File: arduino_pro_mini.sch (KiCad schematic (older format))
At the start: 19 parts, among them J1 CONN_06RA, J2 CONN_12, J3 CONN_02, J4 CONN_02, J5 CONN_12, SW1 SW_Push, U1 MIC5205-2.5YM5, U2 ATmega328-AU, Y1 Resonator_Small

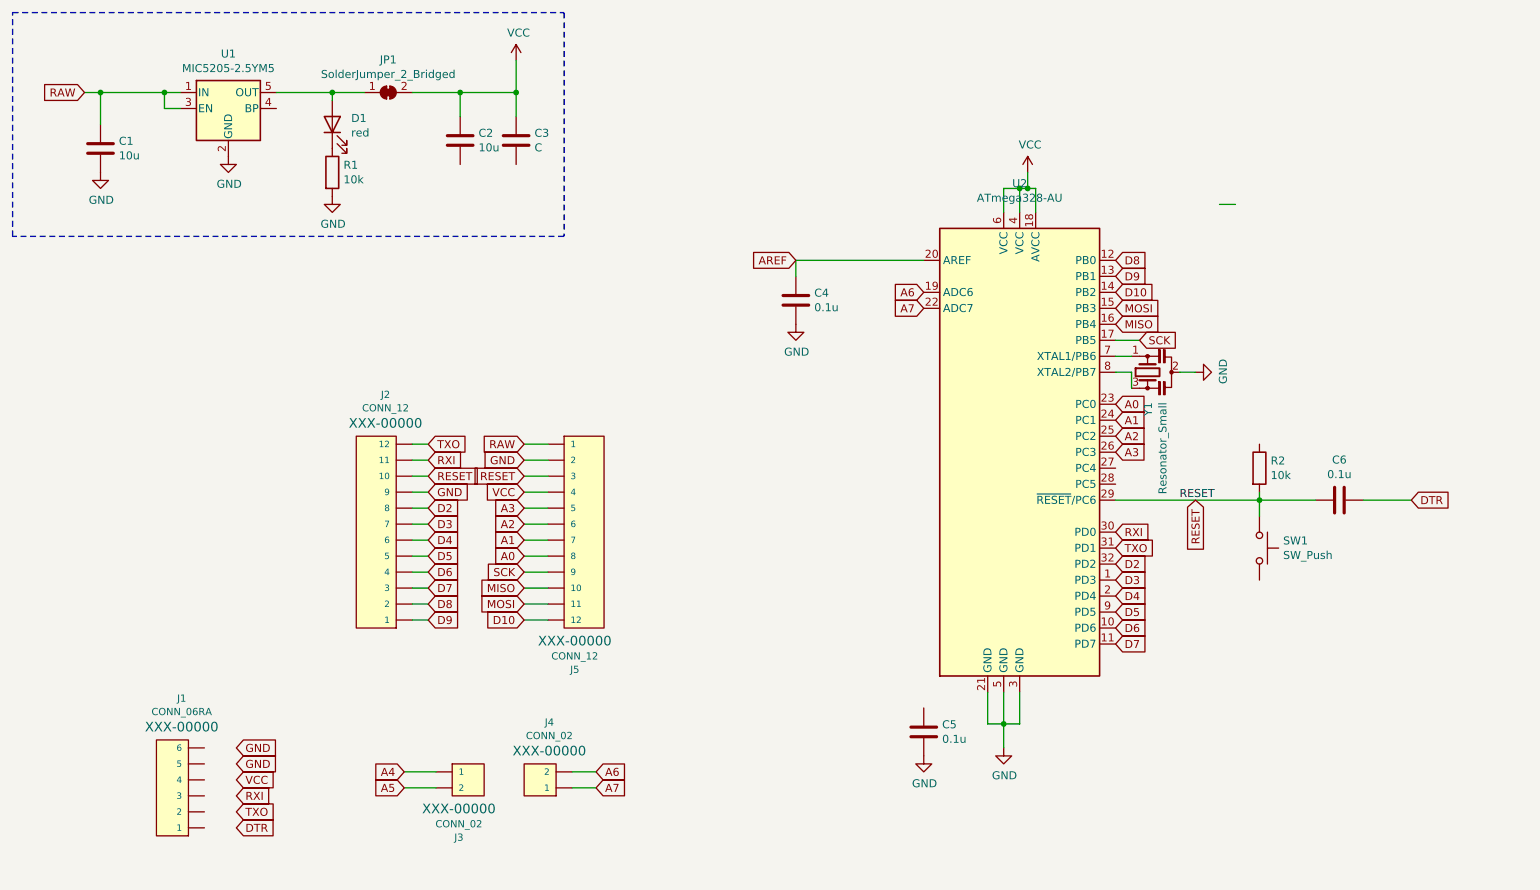
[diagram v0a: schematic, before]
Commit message: complete choose footprint.
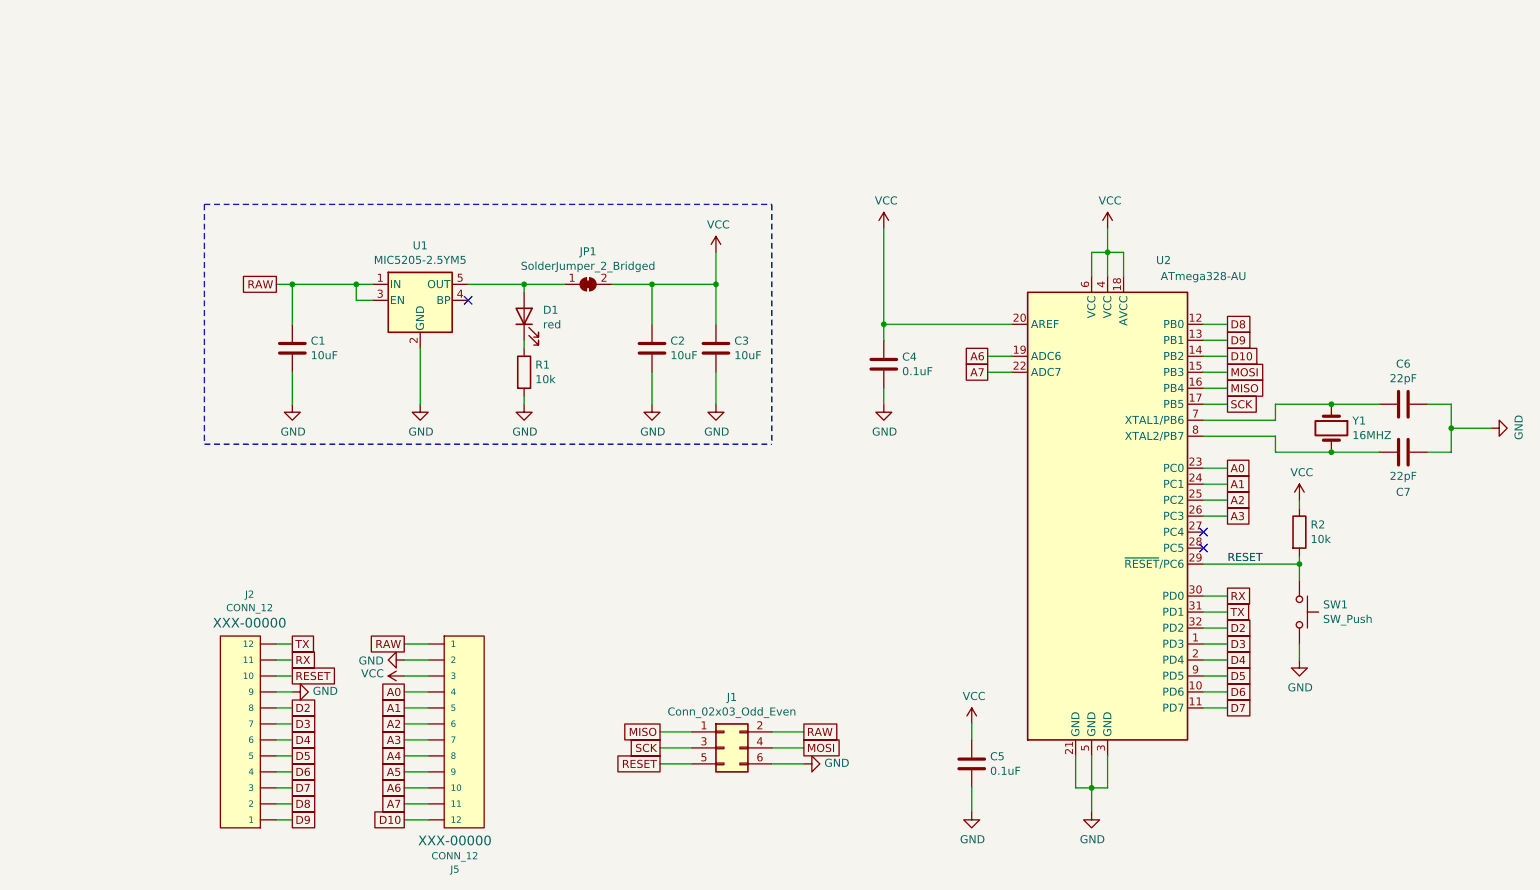
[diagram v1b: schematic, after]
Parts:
- removed J1: CONN_06RA, MOLEX-1X6-RA, symbol KiCadLibs_SparkFun-Kicad-Libraries-master_SparkFun-KiCad-Libraries-master_Libra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
- removed J3, J4: CONN_02, 1X02, symbol KiCadLibs_SparkFun-Kicad-Libraries-master_SparkFun-KiCad-Libraries-master_Libra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
- removed Y1: Resonator_Small, symbol Device:Resonator_Small
- added C7: 22pF, Capacitor_SMD:C_0603_1608Metric, symbol Device:C
- added J1: Conn_02x03_Odd_Even, Pin_Headers:Pin_Header_Straight_2x03, symbol Connector_Generic:Conn_02x03_Odd_Even
- added Y1: 16MHZ, Crystals:Crystal_HC49-U_Vertical, symbol Device:Crystal
- C1, C2: value 10u -> 10uF; footprint (none) -> Capacitor_SMD:C_0603_1608Metric
- C3: value C -> 10uF; footprint (none) -> Capacitor_SMD:C_0603_1608Metric
- C4, C5: value 0.1u -> 0.1uF; footprint (none) -> Capacitor_SMD:C_0603_1608Metric
- C6: value 0.1u -> 22pF; footprint (none) -> Capacitor_SMD:C_0603_1608Metric
- D1: footprint (none) -> LED_SMD:LED_0603_1608Metric
- J2, J5: footprint 1X12 -> Connector_PinHeader_2.54mm:PinHeader_1x12_P2.54mm_Vertical
- JP1: footprint (none) -> Jumper:SolderJumper-2_P1.3mm_Bridged2Bar_Pad1.0x1.5mm
- R1, R2: footprint (none) -> Resistor_SMD:R_0603_1608Metric
- SW1: footprint (none) -> Buttons_Switches_SMD:SW_SPST_PTS645
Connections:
- net AREF is gone; now on net VCC: C4.2, U2.20 (AREF)
- net DTR is gone; now on net GND: C6.2
- net A0: now also J5.4; no longer J5.8
- net A1: now also J5.5; no longer J5.7
- net A3: now also J5.7; no longer J5.5
- net A4: now also J5.8
- net A5: now also J5.9
- net A6: now also J5.10
- net A7: now also J5.11
- net GND: now also C2.2, C3.2, SW1.2, C7.1, J1.6 (Pin_6)
- net MISO: now also J1.1 (Pin_1); no longer J5.10
- net MOSI: now also J1.4 (Pin_4); no longer J5.11
- net RAW: now also J1.2 (Pin_2)
- net RESET: now also J1.5 (Pin_5); no longer C6.1, J5.3
- net SCK: now also J1.3 (Pin_3); no longer J5.9
- net VCC: now also C5.2, J5.3, R2.1; no longer J5.4
- net at U2.7 (XTAL1/PB6): now also C6.1, Y1.1
- net at U2.8 (XTAL2/PB7): now also C7.2, Y1.2
- net RXI renamed RX
- net TXO renamed TX
- no-connect marks 0 -> 3
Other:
- moved on the sheet: C1, C2, C3, C4, C5, D1, J2, J5, JP1, R1, R2, SW1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
